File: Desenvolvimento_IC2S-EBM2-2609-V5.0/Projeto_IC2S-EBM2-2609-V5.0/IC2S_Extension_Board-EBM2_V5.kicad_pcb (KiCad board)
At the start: 4 copper layers, 60 x 60 mm, 141 parts, among them P1 M20-7822046, P2 M20-7821446, U1 TPS7A4001DGN, U10 TPS26613DDFR, U11 TPS26613DDFR, U12 TPS26613DDFR, U13 TPS26613DDFR, U14 TPS7A4001DGN, U2 ADR4525WBRZ-R7, U3 TL431B, U4 MCP1824T-3302E/OT, U5 MCP1824ST-3302E/DB, U6 ISO7141CCDBQR, U7 MCP3208T-BI/SL, U8 TPS26613DDFR, U9 TPS26613DDFR

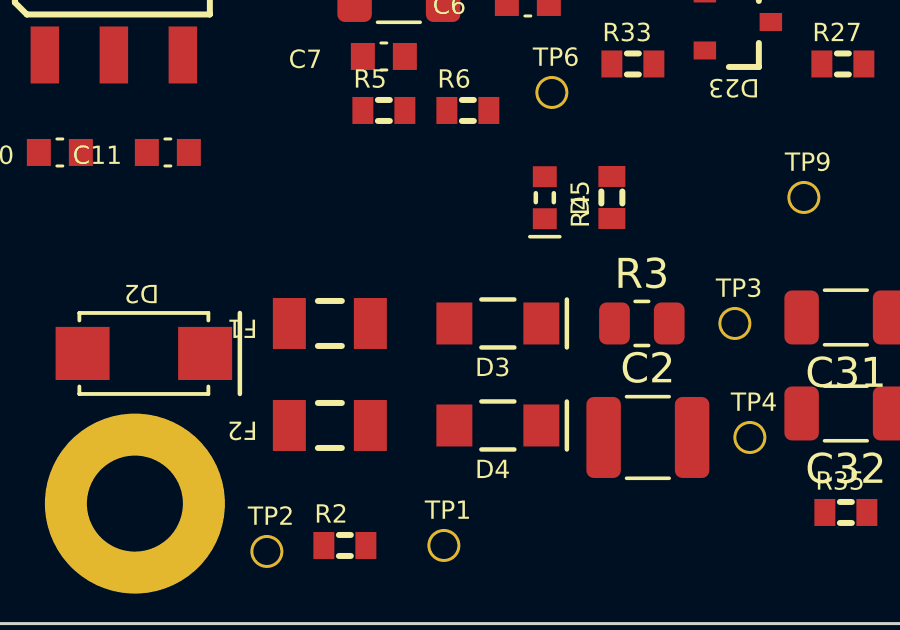
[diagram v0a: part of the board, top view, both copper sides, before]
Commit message: Revisao de 28-09 (vinda da EBM7): ramo unico de 24 V, 100 nF a 50 V, um so MPN de 1 uF
- Saem F1 (250 mA), D3 e R3: o F1 nao aguenta o arranque da placa toda e o R3
  so existia para o limitar. F2 + D4 alimentam o U1 e os lacos; +24V_REG passa
  a +24V_ADC. C1 fica (Cin do TPS7A4001). Esquematico e PCB (sem pistas).
- 100 nF fora do 24 V -> TDK C1608X7R1H104K080AA (50 V); C29 (+24V_ADC) fica
  GRM188R72A104KA35D (100 V). 1 uF -> TDK C1608X7R1H105K080AB.
- Folha 2 notas 3, 11, 13 e 14; BOM preliminar regenerada; README, registo e
  lista de datasheets. Alteracao posterior ao Portao 1, registada como tal.

Co-Authored-By: Claude Opus 5.5 (1M context) <noreply@anthropic.com>
Claude-Session: https://claude.ai/code/session_01KPnkiJQKrkjgRqqw9M78ie
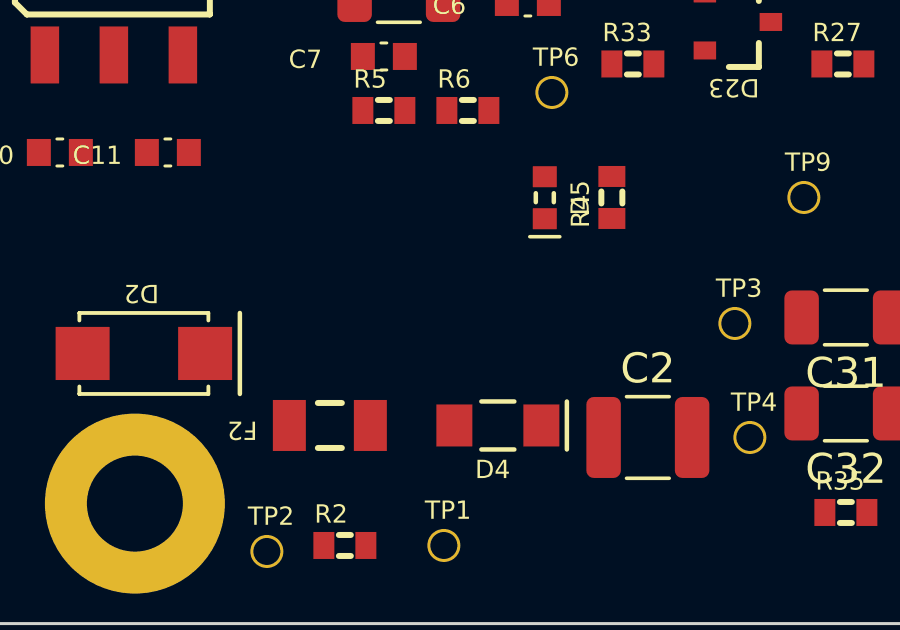
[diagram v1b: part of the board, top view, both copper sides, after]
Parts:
- removed D3: MBR1H100SF, EBM2_V5:SOD123
- removed F1: CC12H250MA-TR, EBM2_V5:1206F
- removed R3: 150R, EBM2_V5:0805R
- C10, C15: value 1uF -> 1uF/50V
- C12, C13, C14, C16, C23, C24, C25, C26, C27, C28, C3, C35, C6, C9: value 100nF -> 100nF/50V
- C17, C18, C19, C20, C21, C22, C34: value 100nF/100V -> 100nF/50V
- TP3: value TP_+24V_REG -> TP_+24V_U1
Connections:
- C1 pad 1: +24V_REG -> +24V_ADC
- TP3 pad 1: +24V_REG -> +24V_ADC
- U1 pad 5: +24V_REG -> +24V_ADC
- U1 pad 8: +24V_REG -> +24V_ADC

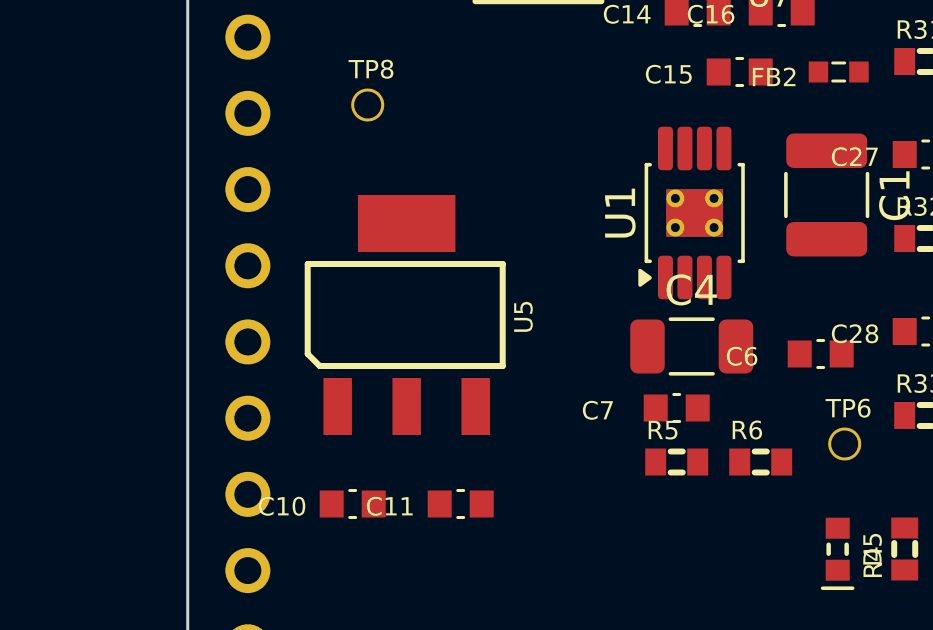
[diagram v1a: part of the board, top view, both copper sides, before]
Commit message: LDO 3,3 V do lado PLC: U5 MCP1824ST (SOT-223) -> MCP1824T-3302E/OT (SOT-23-5), mesmo MPN do U4
- Criterio da equipa: menos MPN, mais pecas do mesmo tipo; o MCP1824ST sai.
- SHDN a VIN, PG aberto; mesmo datasheet (DS22070A), estavel com ceramico >= 1 uF.
- Esquematico: ERC 0; netlist so muda os pinos do U5. PCB: pegada SOT-23-5 no
  mesmo sitio; placa ainda sem pistas; nota 3 da folha 4 actualizada.
- Registo: alteracao_LDO_3V3_lado_PLC_2026-09-28.md (comparacao, verificacao e
  riscos em aberto). BOM e PDF do esquematico regenerados.

Co-Authored-By: Claude Opus 5.5 (1M context) <noreply@anthropic.com>
Claude-Session: https://claude.ai/code/session_01KPnkiJQKrkjgRqqw9M78ie
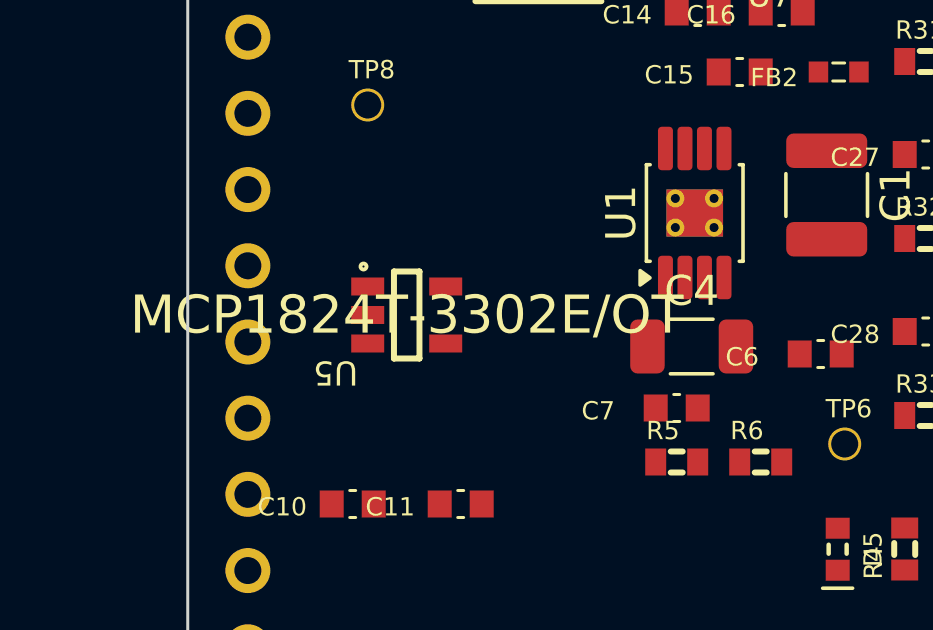
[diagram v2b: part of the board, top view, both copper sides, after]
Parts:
- U5: value MCP1824ST-3302E/DB -> MCP1824T-3302E/OT; footprint EBM2_V5:SOT-223-3 -> EBM2_V5:SOT-23-5
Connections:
- U5 pad 3: +3.3V_DIG -> +5V
- U5 pad 4: DGND -> unconnected-(U5-PG-Pad4)
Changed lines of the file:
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@@
 		)
 	)
+	(footprint "EBM2_V5:SOT-23-5"
+		(layer "F.Cu")
+		(at 125.8 113)
+		(descr "2Solve PCB Library 'SOT-23-5', recuperado da PCB V2.2 (fabricada) em 2026-09-04.")
+		(property "Reference" "U5"
+			(at -1.62301 1.45399 180)
+			(unlocked yes)
+			(layer "F.SilkS")
+			(effects
+				(font
+					(size 0.8 0.8)
+					(thickness 0.107)
+				)
+				(justify left bottom)
+			)
+		)
+		(property "Value" "MCP1824T-3302E/OT"
+			(at -4.2037 5.86359 0)
+			(unlocked yes)
+			(layer "F.SilkS")
+			(hide yes)
+			(effects
+				(font
+					(size 1.524 1.524)
+					(thickness 0.254)
+				)
+				(justify left bottom)
+			)
+		)
+		(property "Datasheet" ""
+			(at 0 0 180)
+			(layer "B.Fab")
+			(hide yes)
+			(effects
+				(font
+					(size 1.27 1.27)
+				)
+				(justify mirror)
+			)
+		)
+		(property "Description" "LDO 3,3 V para VCC1/EN1 do isolador; fecha o G2. Pinos: DS22070A pag. 2 figura"
+			(at 0 0 180)
+			(layer "B.Fab")
+			(hide yes)
+			(effects
+				(font
+					(size 1.27 1.27)
+				)
+				(justify mirror)
+			)
+		)
+		(property "MPN" "MCP1824T-3302E/OT"
+			(at 0 0 0)
+			(layer "F.SilkS")
+			(effects
+				(font
+					(size 1.27 1.27)
+					(thickness 0.15)
+				)
+			)
+		)
+		(sheetfile ".kicad_sch")
+		(attr smd)
+		(duplicate_pad_numbers_are_jumpers no)
+		(fp_line
+			(start -0.425 -1.45)
+			(end -0.425 1.45)
+			(stroke
+				(width 0.2)
+				(type solid)
+			)
+			(layer "F.SilkS")
+		)
+		(fp_line
+			(start -0.425 -1.45)
+			(end 0.425 -1.45)
+			(stroke
+				(width 0.2)
+				(type solid)
+			)
+			(layer "F.SilkS")
+		)
+		(fp_line
+			(start -0.425 1.45)
+			(end 0.425 1.45)
+			(stroke
+				(width 0.2)
+				(type solid)
+			)
+			(layer "F.SilkS")
+		)
+		(fp_line
+			(start 0.425 -1.45)
+			(end 0.425 1.45)
+			(stroke
+				(width 0.2)
+				(type solid)
+			)
+			(layer "F.SilkS")
+		)
+		(fp_circle
+			(center -1.44 -1.616)
+			(end -1.44 -1.516)
+			(stroke
+				(width 0.127)
+				(type solid)
+			)
+			(fill no)
+			(layer "F.SilkS")
+		)
+		(fp_rect
+			(start -2.1 -1.97)
+			(end 2.1 1.7)
+			(stroke
+				(width 0.05)
+				(type default)
+			)
+			(fill no)
+			(layer "F.CrtYd")
+		)
+		(pad "1" smd rect
+			(at -1.3 -0.95)
+			(size 1.1 0.6)
+			(layers "F.Cu" "F.Mask" "F.Paste")
+			(net "+5V")
+		)
+		(pad "2" smd rect
+			(at -1.3 0)
+			(size 1.1 0.6)
+			(layers "F.Cu" "F.Mask" "F.Paste")
+			(net "DGND")
+		)
+		(pad "3" smd rect
+			(at -1.3 0.95)
+			(size 1.1 0.6)
+			(layers "F.Cu" "F.Mask" "F.Paste")
+			(net "+5V")
+		)
+		(pad "4" smd rect
+			(at 1.3 0.95)
+			(size 1.1 0.6)
+			(layers "F.Cu" "F.Mask" "F.Paste")
+			(net "unconnected-(U5-PG-Pad4)")
+		)
+		(pad "5" smd rect
+			(at 1.3 -0.95)
+			(size 1.1 0.6)
+			(layers "F.Cu" "F.Mask" "F.Paste")
+			(net "+3.3V_DIG")
+		)
+		(embedded_fonts no)
+		(embedded_files
+			(file
+				(name "SOT-23-5.step")
+				(type other)
+				(checksum "DB10AC35912B6AC9101E1F1F91780F5E")
+			)
+		)
+		(model "kicad-embed://SOT-23-5.step"
+			(offset
+				(xyz -0.00532 -0.02548 0.51)
+			)
+			(scale
+				(xyz 1 1 1)
+			)
+			(rotate
+				(xyz -90 0 90)
+			)
+		)
+	)
 	(footprint "EBM2_V5:Fiducial_Point_Top-Bot"
 		(layer "F.Cu")
@@
 			)
 		)
-	)
-	(footprint "EBM2_V5:SOT-223-3"
-		(layer "F.Cu")
-		(at 125.8 113)
-		(descr "2Solve PCB Library 'SOT-223-3', recuperado da PCB V2.2 (fabricada) em 2026-09-04.")
-		(property "Reference" "U5"
-			(at 4.265725 0.635 90)
-			(unlocked yes)
-			(layer "F.SilkS")
-			(effects
-				(font
-					(size 0.61 0.61)
-					(thickness 0.102)
-				)
-				(justify left bottom)
-			)
-		)
-		(property "Value" "MCP1824ST-3302E/DB"
-			(at -3.1369 6.57479 0)
-			(unlocked yes)
-			(layer "F.SilkS")
-			(hide yes)
-			(effects
-				(font
-					(size 1.524 1.524)
-					(thickness 0.254)
-				)
-				(justify left bottom)
-			)
-		)
-		(property "Datasheet" ""
-			(at 0 0 0)
-			(layer "F.Fab")
-			(hide yes)
-			(effects
-				(font
-					(size 1.27 1.27)
-				)
-			)
-		)
-		(property "Description" "LDO 3,3 V para VCC1/EN1 do isolador; fecha o G2. Pinos: DS22070A pag. 2 figura"
-			(at 0 0 0)
-			(layer "F.Fab")
-			(hide yes)
-			(effects
-				(font
-					(size 1.27 1.27)
-				)
-			)
-		)
-		(property "MPN" "MCP1824ST-3302E/DB"
-			(at 0 0 0)
-			(layer "F.SilkS")
-			(hide yes)
-			(effects
-				(font
-					(size 1.27 1.27)
-					(thickness 0.15)
-				)
-			)
-		)
-		(sheetname "IC2S_Extension_Board_Model_7-EBM7_V1.1-Load_Cell_4AI")
-		(sheetfile "IC2S_Extension_Board_Model_7-EBM7_V1.1-Load_Cell_4AI.kicad_sch")
-		(attr smd)
-		(duplicate_pad_numbers_are_jumpers no)
-		(fp_line
-			(start -3.3 -1.7)
-			(end 3.2 -1.7)
-			(stroke
-				(width 0.2)
-				(type solid)
-			)
-			(layer "F.SilkS")
-		)
-		(fp_line
-			(start -3.3 1.3)
-			(end -3.3 -1.7)
-			(stroke
-				(width 0.2)
-				(type solid)
-			)
-			(layer "F.SilkS")
-		)
-		(fp_line
-			(start -3.3 1.3)
-			(end -2.9 1.7)
-			(stroke
-				(width 0.2)
-				(type solid)
-			)
-			(layer "F.SilkS")
-		)
-		(fp_line
-			(start -2.9 1.7)
-			(end 3.2 1.7)
-			(stroke
-				(width 0.2)
-				(type solid)
-			)
-			(layer "F.SilkS")
-		)
-		(fp_line
-			(start 3.2 1.7)
-			(end 3.2 -1.7)
-			(stroke
-				(width 0.2)
-				(type solid)
-			)
-			(layer "F.SilkS")
-		)
-		(fp_rect
-			(start -3.55 -4.25)
-			(end 3.45 4.25)
-			(stroke
-				(width 0.05)
-				(type default)
-			)
-			(fill no)
-			(layer "F.CrtYd")
-		)
-		(pad "1" smd rect
-			(at -2.3 3.05 90)
-			(size 1.9 0.95)
-			(layers "F.Cu" "F.Mask" "F.Paste")
-			(net "+5V")
-		)
-		(pad "2" smd rect
-			(at 0 3.05 90)
-			(size 1.9 0.95)
-			(layers "F.Cu" "F.Mask" "F.Paste")
-			(net "DGND")
-		)
-		(pad "3" smd rect
-			(at 2.3 3.05 90)
-			(size 1.9 0.95)
-			(layers "F.Cu" "F.Mask" "F.Paste")
-			(net "+3.3V_DIG")
-		)
-		(pad "4" smd rect
-			(at 0 -3.05 90)
-			(size 1.9 3.25)
-			(layers "F.Cu" "F.Mask" "F.Paste")
-			(net "DGND")
-		)
-		(embedded_fonts no)
-		(embedded_files
-			(file
-				(name "NDT452AP.stp")
-				(type other)
-				(checksum "DC59636768EDDA08F13245DC484E26C6")
-			)
-		)
-		(model "kicad-embed://NDT452AP.stp"
-			(offset
-				(xyz 0 -0 0)
-			)
-			(scale
-				(xyz 1 1 1)
-			)
-			(rotate
-				(xyz -0 -0 -90)
-			)
-		)

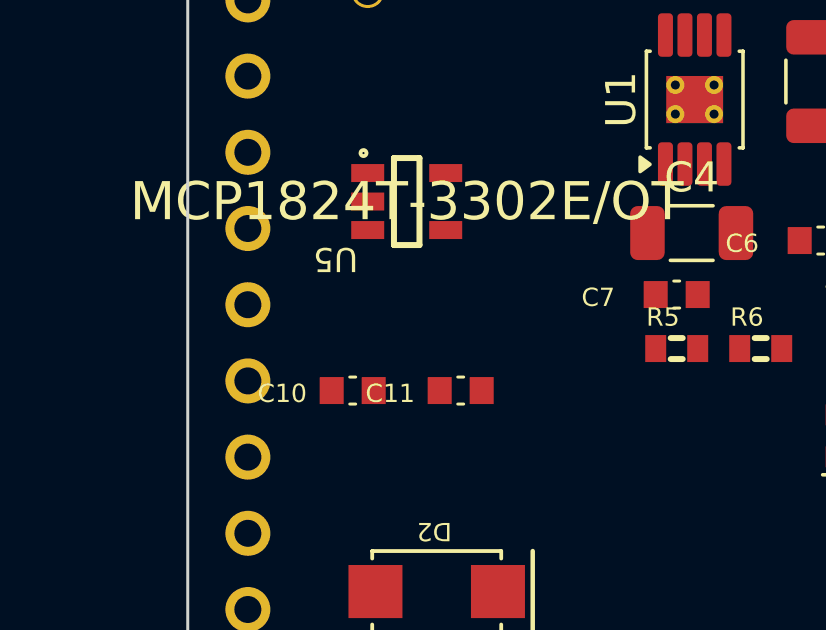
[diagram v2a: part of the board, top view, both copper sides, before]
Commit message: C10 (entrada do U5 MCP1824T) 1 uF -> 10 uF/50 V 1206, o datasheet pede 1-10 uF
- DS22070A p.17: 'a typical input capacitance value of 1 uF to 10 uF'; o 1 uF/50 V dava
  0,80 uF a 5 V no pior caso. Novo: C3216X5R1H106K160AB, o mesmo de C4/C8/C31/C32
  (7,0 uF a 5 V). PCB: clone do C4 a 3,5 mm do U5.
- ERC 0; DRC 0 erros, paridade 0. BOM preliminar e PDF regenerados.

Co-Authored-By: Claude Opus 5.5 (1M context) <noreply@anthropic.com>
Claude-Session: https://claude.ai/code/session_01KPnkiJQKrkjgRqqw9M78ie
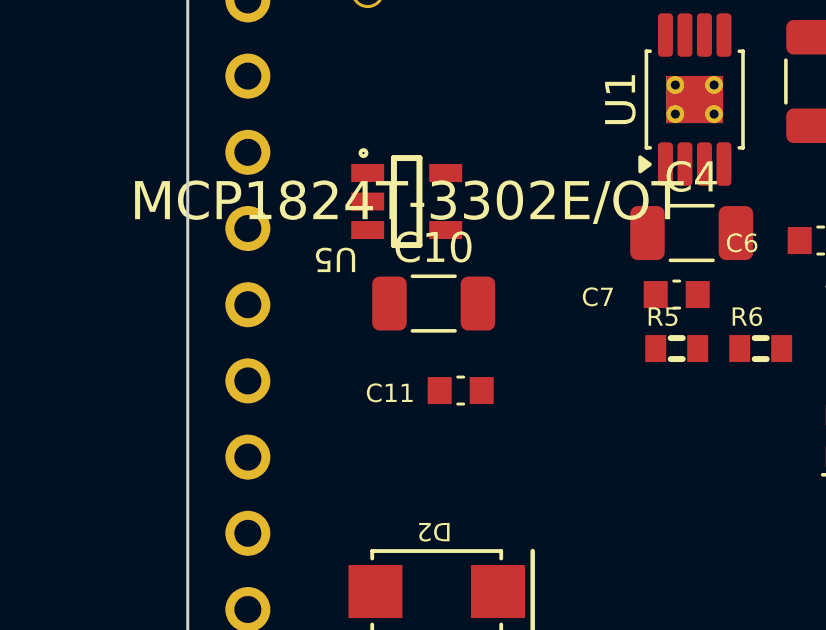
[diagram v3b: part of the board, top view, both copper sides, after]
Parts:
- C10: value 1uF/50V -> 10uF/50V; footprint EBM2_V5:0603C -> EBM2_V5:C_1206_3216Metric
- moved C10 3.96 mm to (126.7, 116.4)
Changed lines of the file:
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@@
 		)
 	)
+	(footprint "EBM2_V5:C_1206_3216Metric"
+		(layer "F.Cu")
+		(at 126.7 116.4)
+		(descr "Capacitor SMD 1206 (3216 Metric), square (rectangular) end terminal, IPC-7351 nominal, (Body size source: IPC-SM-782 page 76, https://www.pcb-3d.com/wordpress/wp-content/uploads/ipc-sm-782a_amendment_1_and_2.pdf) Copiado do KiCad 10 para C50 (CGA5L3X5R1H106M160AB, 10 uF/50 V) em 2026-09-15: o 0805 nao tem stock de 1a linha e o 1206 melhora o DC-bias a 12 V.")
+		(tags "capacitor")
+		(property "Reference" "C10"
+			(at 0 -1.85 0)
+			(layer "F.SilkS")
+			(effects
+				(font
+					(size 1 1)
+					(thickness 0.15)
+				)
+			)
+		)
+		(property "Value" "10uF/50V"
+			(at 0 1.85 0)
+			(layer "F.Fab")
+			(hide yes)
+			(effects
+				(font
+					(size 1 1)
+					(thickness 0.15)
+				)
+			)
+		)
+		(property "Datasheet" ""
+			(at 0 0 0)
+			(layer "F.Fab")
+			(hide yes)
+			(effects
+				(font
+					(size 1.27 1.27)
+				)
+			)
+		)
+		(property "Description" "Entrada do MCP1824T: 10 uF/50 V 1206 (28-09-2026). DS22070A p.17 pede 1-10 uF; o 1 uF dava 0,80 uF a 5 V"
+			(at 0 0 0)
+			(layer "F.Fab")
+			(hide yes)
+			(effects
+				(font
+					(size 1.27 1.27)
+				)
+			)
+		)
+		(property "KiLib_Generator" "SMD_2terminal_chip_molded"
+			(at 0 0 0)
+			(layer "F.SilkS")
+			(hide yes)
+			(effects
+				(font
+					(size 1 1)
+					(thickness 0.15)
+				)
+			)
+		)
+		(property "MPN" "C3216X5R1H106K160AB"
+			(at 0 0 0)
+			(layer "F.SilkS")
+			(hide yes)
+			(effects
+				(font
+					(size 1.27 1.27)
+					(thickness 0.15)
+				)
+			)
+		)
+		(attr smd)
+		(duplicate_pad_numbers_are_jumpers no)
+		(fp_line
+			(start -0.711252 -0.91)
+			(end 0.711252 -0.91)
+			(stroke
+				(width 0.12)
+				(type solid)
+			)
+			(layer "F.SilkS")
+		)
+		(fp_line
+			(start -0.711252 0.91)
+			(end 0.711252 0.91)
+			(stroke
+				(width 0.12)
+				(type solid)
+			)
+			(layer "F.SilkS")
+		)
+		(fp_rect
+			(start -2.3 -1.15)
+			(end 2.3 1.15)
+			(stroke
+				(width 0.05)
+				(type solid)
+			)
+			(fill no)
+			(layer "F.CrtYd")
+		)
+		(fp_rect
+			(start -1.6 -0.8)
+			(end 1.6 0.8)
+			(stroke
+				(width 0.1)
+				(type solid)
+			)
+			(fill no)
+			(layer "F.Fab")
+		)
+		(fp_text user "${REFERENCE}"
+			(at 0 0 0)
+			(layer "F.Fab")
+			(effects
+				(font
+					(size 0.8 0.8)
+					(thickness 0.12)
+				)
+			)
+		)
+		(pad "1" smd roundrect
+			(at -1.475 0)
+			(size 1.15 1.8)
+			(layers "F.Cu" "F.Mask" "F.Paste")
+			(roundrect_rratio 0.217391)
+			(net "+5V")
+		)
+		(pad "2" smd roundrect
+			(at 1.475 0)
+			(size 1.15 1.8)
+			(layers "F.Cu" "F.Mask" "F.Paste")
+			(roundrect_rratio 0.217391)
+			(net "DGND")
+		)
+		(embedded_fonts no)
+		(model "${KICAD10_3DMODEL_DIR}/Capacitor_SMD.3dshapes/C_1206_3216Metric.step"
+			(offset
+				(xyz 0 0 0)
+			)
+			(scale
+				(xyz 1 1 1)
+			)
+			(rotate
+				(xyz 0 0 0)
+			)
+		)
+	)
 	(footprint "EBM2_V5:1206F"
 		(layer "F.Cu")
@@
 			)
 		)
-	)
-	(footprint "EBM2_V5:0603C"
-		(layer "F.Cu")
-		(at 124 119.3)
-		(descr "2Solve PCB Library '0603C', recuperado da PCB V2.2 (fabricada) em 2026-09-04.")
-		(property "Reference" "C10"
-			(at -3.175 0.455725 0)
-			(unlocked yes)
-			(layer "F.SilkS")
-			(effects
-				(font
-					(size 0.61 0.61)
-					(thickness 0.102)
-				)
-				(justify left bottom)
-			)
-		)
-		(property "Value" "1uF/50V"
-			(at -3.72999 -0.3429 270)
-			(unlocked yes)
-			(layer "F.SilkS")
-			(hide yes)
-			(effects
-				(font
-					(size 1.524 1.524)
-					(thickness 0.254)
-				)
-				(justify left bottom)
-			)
-		)
-		(property "Datasheet" ""
-			(at 0 0 0)
-			(layer "F.Fab")
-			(hide yes)
-			(effects
-				(font
-					(size 1.27 1.27)
-				)
-			)
-		)
-		(property "Description" "Entrada do MCP1824S"
-			(at 0 0 0)
-			(layer "F.Fab")
-			(hide yes)
-			(effects
-				(font
-					(size 1.27 1.27)
-				)
-			)
-		)
-		(property "MPN" "C1608X7R1H105K080AB"
-			(at 0 0 0)
-			(layer "F.SilkS")
-			(hide yes)
-			(effects
-				(font
-					(size 1.27 1.27)
-					(thickness 0.15)
-				)
-			)
-		)
-		(sheetname "Load_Cell_Module-V1.0")
-		(sheetfile "Load_Cell_Module-V1.0.kicad_sch")
-		(attr smd)
-		(duplicate_pad_numbers_are_jumpers no)
-		(fp_line
-			(start -0.1 -0.45)
-			(end 0.1 -0.45)
-			(stroke
-				(width 0.1)
-				(type solid)
-			)
-			(layer "F.SilkS")
-		)
-		(fp_line
-			(start -0.1 0.45)
-			(end 0.1 0.45)
-			(stroke
-				(width 0.1)
-				(type solid)
-			)
-			(layer "F.SilkS")
-		)
-		(fp_rect
-			(start -1.35 -0.7)
-			(end 1.35 0.7)
-			(stroke
-				(width 0.05)
-				(type default)
-			)
-			(fill no)
-			(layer "F.CrtYd")
-		)
-		(fp_line
-			(start -0.875 -0.475)
-			(end 0.875 -0.475)
-			(stroke
-				(width 0.1)
-				(type solid)
-			)
-			(layer "User.13")
-		)
-		(fp_line
-			(start -0.875 0.475)
-			(end -0.875 -0.475)
-			(stroke
-				(width 0.1)
-				(type solid)
-			)
-			(layer "User.13")
-		)
-		(fp_line
-			(start -0.875 0.475)
-			(end 0.875 0.475)
-			(stroke
-				(width 0.1)
-				(type solid)
-			)
-			(layer "User.13")
-		)
-		(fp_line
-			(start 0.875 0.475)
-			(end 0.875 -0.475)
-			(stroke
-				(width 0.1)
-				(type solid)
-			)
-			(layer "User.13")
-		)
-		(fp_line
-			(start -1.2 -0.55)
-			(end 1.2 -0.55)
-			(stroke
-				(width 0.1)
-				(type solid)
-			)
-			(layer "User.15")
-		)
-		(fp_line
-			(start -1.2 0.55)
-			(end -1.2 -0.55)
-			(stroke
-				(width 0.1)
-				(type solid)
-			)
-			(layer "User.15")
-		)
-		(fp_line
-			(start -1.2 0.55)
-			(end 1.2 0.55)
-			(stroke
-				(width 0.1)
-				(type solid)
-			)
-			(layer "User.15")
-		)
-		(fp_line
-			(start -0.475 0)
-			(end 0.475 0)
-			(stroke
-				(width 0.1)
-				(type solid)
-			)
-			(layer "User.15")
-		)
-		(fp_line
-			(start 0 0.475)
-			(end 0 -0.475)
-			(stroke
-				(width 0.1)
-				(type solid)
-			)
-			(layer "User.15")
-		)
-		(fp_line
-			(start 1.2 0.55)
-			(end 1.2 -0.55)
-			(stroke
-				(width 0.1)
-				(type solid)
-			)
-			(layer "User.15")
-		)
-		(pad "1" smd rect
-			(at -0.7 0 90)
-			(size 0.9 0.8)
-			(layers "F.Cu" "F.Mask" "F.Paste")
-			(net "+5V")
-		)
-		(pad "2" smd rect
-			(at 0.7 0 90)
-			(size 0.9 0.8)
-			(layers "F.Cu" "F.Mask" "F.Paste")
-			(net "DGND")
-		)
-		(embedded_fonts no)
-		(embedded_files
-			(file
-				(name "User Library-CAPC1608X___CAPC1608X55N.STEP")
-				(type other)
-				(checksum "597E9624E6E4306F77CAACCCC75E6675")
-			)
-		)
-		(model "kicad-embed://User Library-CAPC1608X___CAPC1608X55N.STEP"
-			(offset
-				(xyz 0.00015 0.00016 -0.025)
-			)
-			(scale
-				(xyz 1 1 1)
-			)
-			(rotate
-				(xyz -0 0 0)
-			)
-		)
